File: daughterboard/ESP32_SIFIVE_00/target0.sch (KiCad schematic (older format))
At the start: 0 parts

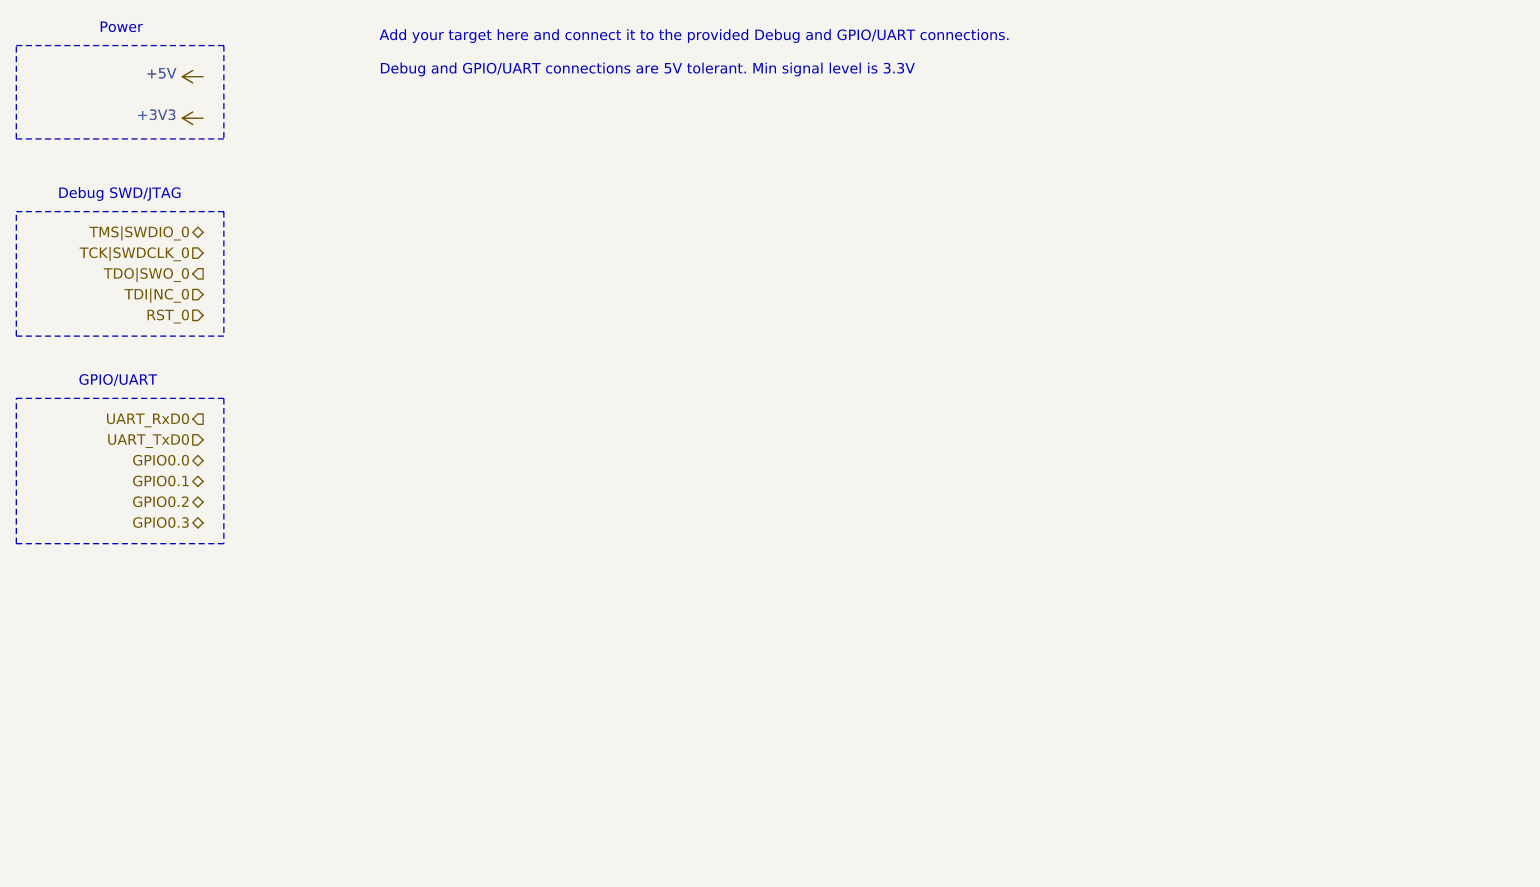
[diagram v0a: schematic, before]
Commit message: finished schematics of ESP32_SIFIVE daughterboard
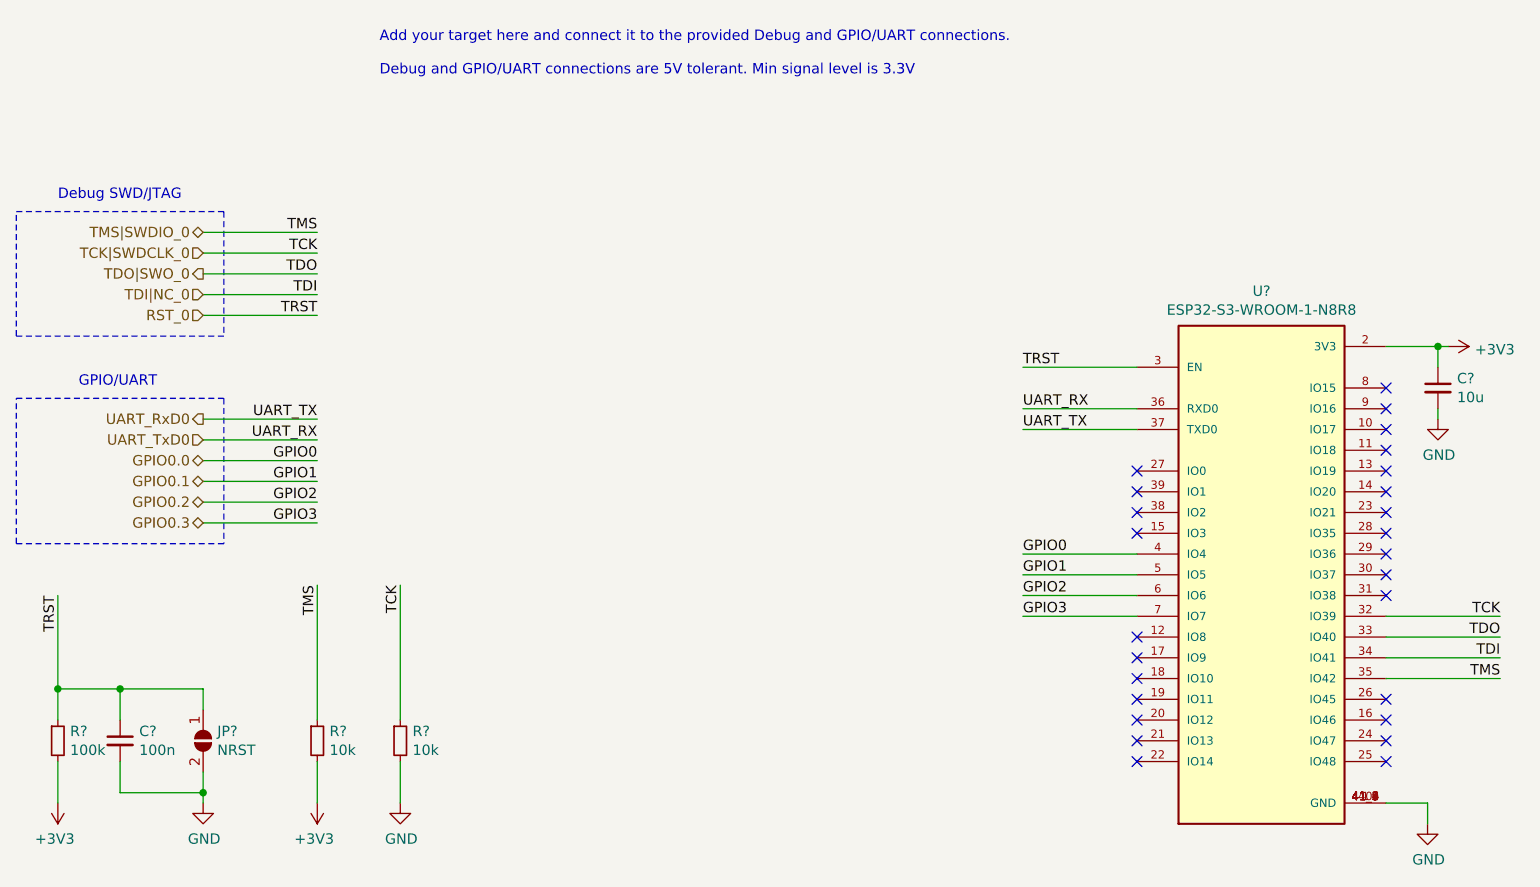
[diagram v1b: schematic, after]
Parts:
- added C?: 100n, symbol Device:C_Small
- added C?: 10u, symbol Device:C_Small
- added JP?: NRST, symbol Jumper:SolderJumper_2_Open
- added R? (x2): 10k, symbol Device:R_Small
- added R?: 100k, symbol Device:R_Small
- added U?: ESP32-S3-WROOM-1-N8R8, hive_daughterboard:XCVR_ESP32-S3-WROOM-1-N8R8, symbol hive_daughterboard:ESP32-S3-WROOM-1-N8R8
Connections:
- net +3V3: now also C?.1, R?.2, R?.2, U?.2 (3V3)
- net GPIO0.0: now also U?.4 (IO4)
- net GPIO0.1: now also U?.5 (IO5)
- net GPIO0.2: now also U?.6 (IO6)
- net GPIO0.3: now also U?.7 (IO7)
- net RST_0: now also C?.1, JP?.1 (A), R?.1, U?.3 (EN)
- net TCK|SWDCLK_0: now also R?.1, U?.32 (IO39)
- net TDI|NC_0: now also U?.34 (IO41)
- net TDO|SWO_0: now also U?.33 (IO40)
- net TMS|SWDIO_0: now also R?.1, U?.35 (IO42)
- net UART_RxD0: now also U?.37 (TXD0)
- net UART_TxD0: now also U?.36 (RXD0)
- new net GND: C?.2, C?.2, JP?.2 (B), R?.2, U?.1 (GND), U?.40 (GND), U?.41_1 (GND), U?.41_2 (GND), U?.41_3 (GND), U?.41_4 (GND), U?.41_5 (GND), U?.41_6 (GND), U?.41_7 (GND), U?.41_8 (GND), U?.41_9 (GND)
- no-connect marks 0 -> 26
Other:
- note removed: "Power"

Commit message: ERC on daughterboards
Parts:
- gave numbers to parts that had none: 7
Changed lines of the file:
@@
 Add your target here and connect it to the provided Debug and GPIO/UART connections.\n\nDebug and GPIO/UART connections are 5V tolerant. Min signal level is 3.3V
 $Comp
-L hive_daughterboard:ESP32-S3-WROOM-1-N8R8 U?
+L hive_daughterboard:ESP32-S3-WROOM-1-N8R8 U0
 U 1 1 618F6A48
 P 6800 3300
-F 0 "U?" H 6800 4667 50  0000 C CNN
+F 0 "U0" H 6800 4667 50  0000 C CNN
 F 1 "ESP32-S3-WROOM-1-N8R8" H 6800 4576 50  0000 C CNN
 F 2 "hive_daughterboard:XCVR_ESP32-S3-WROOM-1-N8R8" H 6800 3300 50  0001 L BNN
@@
 GPIO3
 $Comp
-L power:GND #PWR?
+L power:GND #PWR0129
 U 1 1 618FE06A
 P 7600 4500
-F 0 "#PWR?" H 7600 4250 50  0001 C CNN
+F 0 "#PWR0129" H 7600 4250 50  0001 C CNN
 F 1 "GND" H 7605 4327 50  0000 C CNN
 F 2 "" H 7600 4500 50  0001 C CNN
@@
 	7600 4400 7600 4500
 $Comp
-L power:+3V3 #PWR?
+L power:+3V3 #PWR0130
 U 1 1 6190047A
 P 7700 2200
-F 0 "#PWR?" H 7700 2050 50  0001 C CNN
+F 0 "#PWR0130" H 7700 2050 50  0001 C CNN
 F 1 "+3V3" V 7715 2328 50  0000 L CNN
 F 2 "" H 7700 2200 50  0001 C CNN
@@
 P 2650 4100
 AR Path="/616688D6/6190BB9E" Ref="R?"  Part="1"
-AR Path="/61668514/6190BB9E" Ref="R?"  Part="1"
-F 0 "R?" H 2709 4146 50  0000 L CNN
+AR Path="/61668514/6190BB9E" Ref="R10"  Part="1"
+F 0 "R10" H 2709 4146 50  0000 L CNN
 F 1 "10k" H 2709 4055 50  0000 L CNN
 F 2 "" H 2650 4100 50  0001 C CNN
@@
 P 2650 4400
 AR Path="/616688D6/6190BBA4" Ref="#PWR?"  Part="1"
-AR Path="/61668514/6190BBA4" Ref="#PWR?"  Part="1"
-F 0 "#PWR?" H 2650 4150 50  0001 C CNN
+AR Path="/61668514/6190BBA4" Ref="#PWR0131"  Part="1"
+F 0 "#PWR0131" H 2650 4150 50  0001 C CNN
 F 1 "GND" H 2655 4227 50  0000 C CNN
 F 2 "" H 2650 4400 50  0001 C CNN
@@
 P 2250 4100
 AR Path="/616688D6/6190BBAC" Ref="R?"  Part="1"
-AR Path="/61668514/6190BBAC" Ref="R?"  Part="1"
-F 0 "R?" H 2309 4146 50  0000 L CNN
+AR Path="/61668514/6190BBAC" Ref="R9"  Part="1"
+F 0 "R9" H 2309 4146 50  0000 L CNN
 F 1 "10k" H 2309 4055 50  0000 L CNN
 F 2 "" H 2250 4100 50  0001 C CNN
@@
 P 2250 4400
 AR Path="/616688D6/6190BBB4" Ref="#PWR?"  Part="1"
-AR Path="/61668514/6190BBB4" Ref="#PWR?"  Part="1"
-F 0 "#PWR?" H 2250 4250 50  0001 C CNN
+AR Path="/61668514/6190BBB4" Ref="#PWR0132"  Part="1"
+F 0 "#PWR0132" H 2250 4250 50  0001 C CNN
 F 1 "+3V3" H 2265 4573 50  0000 C CNN
 F 2 "" H 2250 4400 50  0001 C CNN
@@
 AR Path="/616688D6/61910374" Ref="R?"  Part="1"
 AR Path="/61668157/61910374" Ref="R?"  Part="1"
-F 0 "R?" H 1059 4146 50  0000 L CNN
+AR Path="/61668514/61910374" Ref="R8"  Part="1"
+F 0 "R8" H 1059 4146 50  0000 L CNN
 F 1 "100k" H 1059 4055 50  0000 L CNN
 F 2 "" H 1000 4100 50  0001 C CNN
@@
 $EndComp
 $Comp
-L Jumper:SolderJumper_2_Open JP?
+L Jumper:SolderJumper_2_Open JP3
 U 1 1 6191037A
 P 1700 4100
-F 0 "JP?" V 1654 4168 50  0000 L CNN
+F 0 "JP3" V 1654 4168 50  0000 L CNN
 F 1 "NRST" V 1745 4168 50  0000 L CNN
 F 2 "" H 1700 4100 50  0001 C CNN
@@
 $EndComp
 $Comp
-L power:+3V3 #PWR?
+L power:+3V3 #PWR0133
 U 1 1 61910380
 P 1000 4400
-F 0 "#PWR?" H 1000 4250 50  0001 C CNN
+F 0 "#PWR0133" H 1000 4250 50  0001 C CNN
 F 1 "+3V3" H 1015 4573 50  0000 C CNN
 F 2 "" H 1000 4400 50  0001 C CNN
@@
 	1000 3400 1000 3850
 $Comp
-L power:GND #PWR?
+L power:GND #PWR0134
 U 1 1 6191038A
 P 1700 4400
-F 0 "#PWR?" H 1700 4150 50  0001 C CNN
+F 0 "#PWR0134" H 1700 4150 50  0001 C CNN
 F 1 "GND" H 1705 4227 50  0000 C CNN
 F 2 "" H 1700 4400 50  0001 C CNN
@@
 TRST
 $Comp
-L Device:C_Small C?
+L Device:C_Small C13
 U 1 1 61910391
 P 1300 4100
-F 0 "C?" H 1392 4146 50  0000 L CNN
+F 0 "C13" H 1392 4146 50  0000 L CNN
 F 1 "100n" H 1392 4055 50  0000 L CNN
 F 2 "" H 1300 4100 50  0001 C CNN
@@
 GPIO3
 $Comp
-L Device:C_Small C?
+L Device:C_Small C14
 U 1 1 6191C99F
 P 7650 2400
-F 0 "C?" H 7742 2446 50  0000 L CNN
+F 0 "C14" H 7742 2446 50  0000 L CNN
 F 1 "10u" H 7742 2355 50  0000 L CNN
 F 2 "" H 7650 2400 50  0001 C CNN
@@
 	7650 2200 7400 2200
 $Comp
-L power:GND #PWR?
+L power:GND #PWR0135
 U 1 1 6191E673
 P 7650 2550
-F 0 "#PWR?" H 7650 2300 50  0001 C CNN
+F 0 "#PWR0135" H 7650 2300 50  0001 C CNN
 F 1 "GND" H 7655 2377 50  0000 C CNN
 F 2 "" H 7650 2550 50  0001 C CNN

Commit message: added testpoints to daughterboards, updated readme
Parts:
- added TP12: TMS, symbol Connector:TestPoint
- added TP13: TCK, symbol Connector:TestPoint
- added TP14: TDO, symbol Connector:TestPoint
- added TP15: TDI, symbol Connector:TestPoint
- added TP16: TRST, symbol Connector:TestPoint
- added TP17: UART_TX, symbol Connector:TestPoint
- added TP18: UART_RX, symbol Connector:TestPoint
- added TP19: GPIO0, symbol Connector:TestPoint
- added TP20: GPIO1, symbol Connector:TestPoint
- added TP21: GPIO2, symbol Connector:TestPoint
- added TP22: GPIO3, symbol Connector:TestPoint
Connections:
- net GPIO0.0: now also TP19.1
- net GPIO0.1: now also TP20.1
- net GPIO0.2: now also TP21.1
- net GPIO0.3: now also TP22.1
- net RST_0: now also TP16.1
- net TCK|SWDCLK_0: now also TP13.1
- net TDI|NC_0: now also TP15.1
- net TDO|SWO_0: now also TP14.1
- net TMS|SWDIO_0: now also TP12.1
- net UART_RxD0: now also TP17.1
- net UART_TxD0: now also TP18.1
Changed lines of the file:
@@
 NoConn ~ 6200 2900
 NoConn ~ 6200 2800
+$Comp
+L Connector:TestPoint TP?
+U 1 1 61913AED
+P 2250 1650
+AR Path="/616688D6/61913AED" Ref="TP?"  Part="1"
+AR Path="/61668514/61913AED" Ref="TP12"  Part="1"
+F 0 "TP12" V 2250 1850 50  0000 L CNN
+F 1 "TMS" V 2250 2150 50  0000 L CNN
+F 2 "" H 2450 1650 50  0001 C CNN
+F 3 "~" H 2450 1650 50  0001 C CNN
+	1    2250 1650
+	0    1    1    0
+$EndComp
+$Comp
+L Connector:TestPoint TP?
+U 1 1 61913AF3
+P 2250 1750
+AR Path="/616688D6/61913AF3" Ref="TP?"  Part="1"
+AR Path="/61668514/61913AF3" Ref="TP13"  Part="1"
+F 0 "TP13" V 2250 1950 50  0000 L CNN
+F 1 "TCK" V 2250 2250 50  0000 L CNN
+F 2 "" H 2450 1750 50  0001 C CNN
+F 3 "~" H 2450 1750 50  0001 C CNN
+	1    2250 1750
+	0    1    1    0
+$EndComp
+$Comp
+L Connector:TestPoint TP?
+U 1 1 61913AF9
+P 2250 1850
+AR Path="/616688D6/61913AF9" Ref="TP?"  Part="1"
+AR Path="/61668514/61913AF9" Ref="TP14"  Part="1"
+F 0 "TP14" V 2250 2050 50  0000 L CNN
+F 1 "TDO" V 2250 2350 50  0000 L CNN
+F 2 "" H 2450 1850 50  0001 C CNN
+F 3 "~" H 2450 1850 50  0001 C CNN
+	1    2250 1850
+	0    1    1    0
+$EndComp
+$Comp
+L Connector:TestPoint TP?
+U 1 1 61913AFF
+P 2250 1950
+AR Path="/616688D6/61913AFF" Ref="TP?"  Part="1"
+AR Path="/61668514/61913AFF" Ref="TP15"  Part="1"
+F 0 "TP15" V 2250 2150 50  0000 L CNN
+F 1 "TDI" V 2250 2450 50  0000 L CNN
+F 2 "" H 2450 1950 50  0001 C CNN
+F 3 "~" H 2450 1950 50  0001 C CNN
+	1    2250 1950
+	0    1    1    0
+$EndComp
+$Comp
+L Connector:TestPoint TP?
+U 1 1 61913B05
+P 2250 2050
+AR Path="/616688D6/61913B05" Ref="TP?"  Part="1"
+AR Path="/61668514/61913B05" Ref="TP16"  Part="1"
+F 0 "TP16" V 2250 2250 50  0000 L CNN
+F 1 "TRST" V 2250 2550 50  0000 L CNN
+F 2 "" H 2450 2050 50  0001 C CNN
+F 3 "~" H 2450 2050 50  0001 C CNN
+	1    2250 2050
+	0    1    1    0
+$EndComp
+$Comp
+L Connector:TestPoint TP?
+U 1 1 61913B0B
+P 2250 2550
+AR Path="/616688D6/61913B0B" Ref="TP?"  Part="1"
+AR Path="/61668514/61913B0B" Ref="TP17"  Part="1"
+F 0 "TP17" V 2250 2750 50  0000 L CNN
+F 1 "UART_TX" V 2250 3050 50  0000 L CNN
+F 2 "" H 2450 2550 50  0001 C CNN
+F 3 "~" H 2450 2550 50  0001 C CNN
+	1    2250 2550
+	0    1    1    0
+$EndComp
+$Comp
+L Connector:TestPoint TP?
+U 1 1 61913B11
+P 2250 2650
+AR Path="/616688D6/61913B11" Ref="TP?"  Part="1"
+AR Path="/61668514/61913B11" Ref="TP18"  Part="1"
+F 0 "TP18" V 2250 2850 50  0000 L CNN
+F 1 "UART_RX" V 2250 3150 50  0000 L CNN
+F 2 "" H 2450 2650 50  0001 C CNN
+F 3 "~" H 2450 2650 50  0001 C CNN
+	1    2250 2650
+	0    1    1    0
+$EndComp
+$Comp
+L Connector:TestPoint TP?
+U 1 1 61913B17
+P 2250 2750
+AR Path="/616688D6/61913B17" Ref="TP?"  Part="1"
+AR Path="/61668514/61913B17" Ref="TP19"  Part="1"
+F 0 "TP19" V 2250 2950 50  0000 L CNN
+F 1 "GPIO0" V 2250 3250 50  0000 L CNN
+F 2 "" H 2450 2750 50  0001 C CNN
+F 3 "~" H 2450 2750 50  0001 C CNN
+	1    2250 2750
+	0    1    1    0
+$EndComp
+$Comp
+L Connector:TestPoint TP?
+U 1 1 61913B1D
+P 2250 2850
+AR Path="/616688D6/61913B1D" Ref="TP?"  Part="1"
+AR Path="/61668514/61913B1D" Ref="TP20"  Part="1"
+F 0 "TP20" V 2250 3050 50  0000 L CNN
+F 1 "GPIO1" V 2250 3350 50  0000 L CNN
+F 2 "" H 2450 2850 50  0001 C CNN
+F 3 "~" H 2450 2850 50  0001 C CNN
+	1    2250 2850
+	0    1    1    0
+$EndComp
+$Comp
+L Connector:TestPoint TP?
+U 1 1 61913B23
+P 2250 2950
+AR Path="/616688D6/61913B23" Ref="TP?"  Part="1"
+AR Path="/61668514/61913B23" Ref="TP21"  Part="1"
+F 0 "TP21" V 2250 3150 50  0000 L CNN
+F 1 "GPIO2" V 2250 3450 50  0000 L CNN
+F 2 "" H 2450 2950 50  0001 C CNN
+F 3 "~" H 2450 2950 50  0001 C CNN
+	1    2250 2950
+	0    1    1    0
+$EndComp
+$Comp
+L Connector:TestPoint TP?
+U 1 1 61913B29
+P 2250 3050
+AR Path="/616688D6/61913B29" Ref="TP?"  Part="1"
+AR Path="/61668514/61913B29" Ref="TP22"  Part="1"
+F 0 "TP22" V 2250 3250 50  0000 L CNN
+F 1 "GPIO3" V 2250 3550 50  0000 L CNN
+F 2 "" H 2450 3050 50  0001 C CNN
+F 3 "~" H 2450 3050 50  0001 C CNN
+	1    2250 3050
+	0    1    1    0
+$EndComp
 $EndSCHEMATC

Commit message: started with esp32/sifive layout
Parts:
- removed TP16: TRST, symbol Connector:TestPoint
- removed TP19: GPIO0, symbol Connector:TestPoint
- removed TP20: GPIO1, symbol Connector:TestPoint
- removed TP21: GPIO2, symbol Connector:TestPoint
- removed TP22: GPIO3, symbol Connector:TestPoint
- C13, C14: footprint (none) -> Capacitor_SMD:C_0603_1608Metric_Pad1.05x0.95mm_HandSolder
- JP3: footprint (none) -> Jumper:SolderJumper-2_P1.3mm_Open_TrianglePad1.0x1.5mm
- R10, R8, R9: footprint (none) -> Resistor_SMD:R_0603_1608Metric_Pad1.05x0.95mm_HandSolder
- TP12, TP13, TP14, TP15, TP17, TP18: footprint (none) -> TestPoint:TestPoint_Pad_1.0x1.0mm
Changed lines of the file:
@@
 F 0 "R10" H 2709 4146 50  0000 L CNN
 F 1 "10k" H 2709 4055 50  0000 L CNN
-F 2 "" H 2650 4100 50  0001 C CNN
+F 2 "Resistor_SMD:R_0603_1608Metric_Pad1.05x0.95mm_HandSolder" H 2650 4100 50  0001 C CNN
 F 3 "~" H 2650 4100 50  0001 C CNN
 	1    2650 4100
@@
 F 0 "R9" H 2309 4146 50  0000 L CNN
 F 1 "10k" H 2309 4055 50  0000 L CNN
-F 2 "" H 2250 4100 50  0001 C CNN
+F 2 "Resistor_SMD:R_0603_1608Metric_Pad1.05x0.95mm_HandSolder" H 2250 4100 50  0001 C CNN
 F 3 "~" H 2250 4100 50  0001 C CNN
 	1    2250 4100
@@
 F 0 "R8" H 1059 4146 50  0000 L CNN
 F 1 "100k" H 1059 4055 50  0000 L CNN
-F 2 "" H 1000 4100 50  0001 C CNN
+F 2 "Resistor_SMD:R_0603_1608Metric_Pad1.05x0.95mm_HandSolder" H 1000 4100 50  0001 C CNN
 F 3 "~" H 1000 4100 50  0001 C CNN
 	1    1000 4100
@@
 F 0 "JP3" V 1654 4168 50  0000 L CNN
 F 1 "NRST" V 1745 4168 50  0000 L CNN
-F 2 "" H 1700 4100 50  0001 C CNN
+F 2 "Jumper:SolderJumper-2_P1.3mm_Open_TrianglePad1.0x1.5mm" H 1700 4100 50  0001 C CNN
 F 3 "~" H 1700 4100 50  0001 C CNN
 	1    1700 4100
@@
 F 0 "C13" H 1392 4146 50  0000 L CNN
 F 1 "100n" H 1392 4055 50  0000 L CNN
-F 2 "" H 1300 4100 50  0001 C CNN
+F 2 "Capacitor_SMD:C_0603_1608Metric_Pad1.05x0.95mm_HandSolder" H 1300 4100 50  0001 C CNN
 F 3 "~" H 1300 4100 50  0001 C CNN
 	1    1300 4100
@@
 F 0 "C14" H 7742 2446 50  0000 L CNN
 F 1 "10u" H 7742 2355 50  0000 L CNN
-F 2 "" H 7650 2400 50  0001 C CNN
+F 2 "Capacitor_SMD:C_0603_1608Metric_Pad1.05x0.95mm_HandSolder" H 7650 2400 50  0001 C CNN
 F 3 "~" H 7650 2400 50  0001 C CNN
 	1    7650 2400
@@
 F 0 "TP12" V 2250 1850 50  0000 L CNN
 F 1 "TMS" V 2250 2150 50  0000 L CNN
-F 2 "" H 2450 1650 50  0001 C CNN
+F 2 "TestPoint:TestPoint_Pad_1.0x1.0mm" H 2450 1650 50  0001 C CNN
 F 3 "~" H 2450 1650 50  0001 C CNN
 	1    2250 1650
@@
 F 0 "TP13" V 2250 1950 50  0000 L CNN
 F 1 "TCK" V 2250 2250 50  0000 L CNN
-F 2 "" H 2450 1750 50  0001 C CNN
+F 2 "TestPoint:TestPoint_Pad_1.0x1.0mm" H 2450 1750 50  0001 C CNN
 F 3 "~" H 2450 1750 50  0001 C CNN
 	1    2250 1750
@@
 F 0 "TP14" V 2250 2050 50  0000 L CNN
 F 1 "TDO" V 2250 2350 50  0000 L CNN
-F 2 "" H 2450 1850 50  0001 C CNN
+F 2 "TestPoint:TestPoint_Pad_1.0x1.0mm" H 2450 1850 50  0001 C CNN
 F 3 "~" H 2450 1850 50  0001 C CNN
 	1    2250 1850
@@
 F 0 "TP15" V 2250 2150 50  0000 L CNN
 F 1 "TDI" V 2250 2450 50  0000 L CNN
-F 2 "" H 2450 1950 50  0001 C CNN
+F 2 "TestPoint:TestPoint_Pad_1.0x1.0mm" H 2450 1950 50  0001 C CNN
 F 3 "~" H 2450 1950 50  0001 C CNN
 	1    2250 1950
-	0    1    1    0
-$EndComp
-$Comp
-L Connector:TestPoint TP?
-U 1 1 61913B05
-P 2250 2050
-AR Path="/616688D6/61913B05" Ref="TP?"  Part="1"
-AR Path="/61668514/61913B05" Ref="TP16"  Part="1"
-F 0 "TP16" V 2250 2250 50  0000 L CNN
-F 1 "TRST" V 2250 2550 50  0000 L CNN
-F 2 "" H 2450 2050 50  0001 C CNN
-F 3 "~" H 2450 2050 50  0001 C CNN
-	1    2250 2050
 	0    1    1    0
 $EndComp
@@
 F 0 "TP17" V 2250 2750 50  0000 L CNN
 F 1 "UART_TX" V 2250 3050 50  0000 L CNN
-F 2 "" H 2450 2550 50  0001 C CNN
+F 2 "TestPoint:TestPoint_Pad_1.0x1.0mm" H 2450 2550 50  0001 C CNN
 F 3 "~" H 2450 2550 50  0001 C CNN
 	1    2250 2550
@@
 F 0 "TP18" V 2250 2850 50  0000 L CNN
 F 1 "UART_RX" V 2250 3150 50  0000 L CNN
-F 2 "" H 2450 2650 50  0001 C CNN
+F 2 "TestPoint:TestPoint_Pad_1.0x1.0mm" H 2450 2650 50  0001 C CNN
 F 3 "~" H 2450 2650 50  0001 C CNN
 	1    2250 2650
 	0    1    1    0
 $EndComp
-$Comp
-L Connector:TestPoint TP?
-U 1 1 61913B17
-P 2250 2750
-AR Path="/616688D6/61913B17" Ref="TP?"  Part="1"
-AR Path="/61668514/61913B17" Ref="TP19"  Part="1"
-F 0 "TP19" V 2250 2950 50  0000 L CNN
-F 1 "GPIO0" V 2250 3250 50  0000 L CNN
-F 2 "" H 2450 2750 50  0001 C CNN
-F 3 "~" H 2450 2750 50  0001 C CNN
-	1    2250 2750
-	0    1    1    0
-$EndComp
-$Comp
-L Connector:TestPoint TP?
-U 1 1 61913B1D
-P 2250 2850
-AR Path="/616688D6/61913B1D" Ref="TP?"  Part="1"
-AR Path="/61668514/61913B1D" Ref="TP20"  Part="1"
-F 0 "TP20" V 2250 3050 50  0000 L CNN
-F 1 "GPIO1" V 2250 3350 50  0000 L CNN
-F 2 "" H 2450 2850 50  0001 C CNN
-F 3 "~" H 2450 2850 50  0001 C CNN
-	1    2250 2850
-	0    1    1    0
-$EndComp
-$Comp
-L Connector:TestPoint TP?
-U 1 1 61913B23
-P 2250 2950
-AR Path="/616688D6/61913B23" Ref="TP?"  Part="1"
-AR Path="/61668514/61913B23" Ref="TP21"  Part="1"
-F 0 "TP21" V 2250 3150 50  0000 L CNN
-F 1 "GPIO2" V 2250 3450 50  0000 L CNN
-F 2 "" H 2450 2950 50  0001 C CNN
-F 3 "~" H 2450 2950 50  0001 C CNN
-	1    2250 2950
-	0    1    1    0
-$EndComp
-$Comp
-L Connector:TestPoint TP?
-U 1 1 61913B29
-P 2250 3050
-AR Path="/616688D6/61913B29" Ref="TP?"  Part="1"
-AR Path="/61668514/61913B29" Ref="TP22"  Part="1"
-F 0 "TP22" V 2250 3250 50  0000 L CNN
-F 1 "GPIO3" V 2250 3550 50  0000 L CNN
-F 2 "" H 2450 3050 50  0001 C CNN
-F 3 "~" H 2450 3050 50  0001 C CNN
-	1    2250 3050
-	0    1    1    0
-$EndComp
